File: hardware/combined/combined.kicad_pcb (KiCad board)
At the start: 2 copper layers, 62.1 x 208.5 mm, 143 parts, among them J1 USB-C 5V in, J2 Mini-DIN-8 to printer, J4 Mini-DIN-8 LocalTalk, SW1 EVQP44B3M, SW2 B3U-1000P, SW3 TS-1002-BR16026, U1 ESP32-S3-WROOM-1-N8R2, U2 SP3490EN-L, U3 SP3232EEN, U4 AP7361C-33E, U5 USBLC6-2SC6, U6 SP3485EN-L, U7 PIC12F1840-I/P, U8 SP3485EN-L, U9 74AHCT1G125SE-7

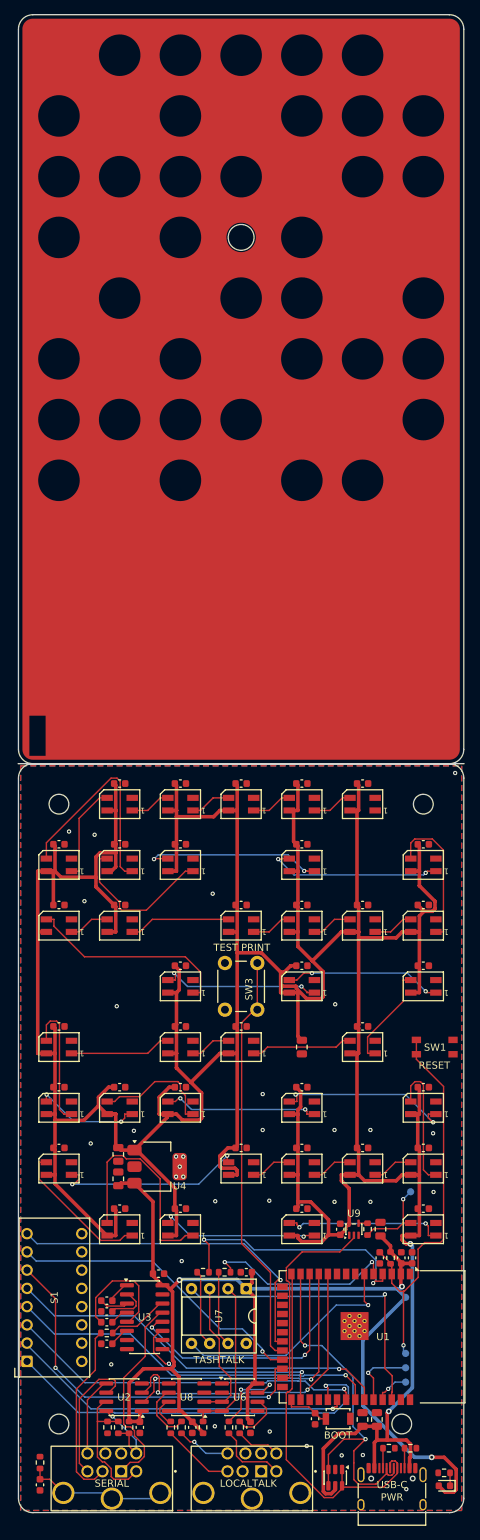
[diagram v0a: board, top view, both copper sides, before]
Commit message: Panel: test hole 3.6 -> 3.8mm for the TS-1002's 3.5+/-0.2mm shaft
Datasheet-verified: the switch is 16.0mm tall (correct for 0.5-1mm proud at
a 13.4-13.9mm lattice) but its shaft is 3.5mm — 3.6 left 0.05mm/side and a
tolerance-stack bind. Wells chose the bigger hole over a printed plunger.
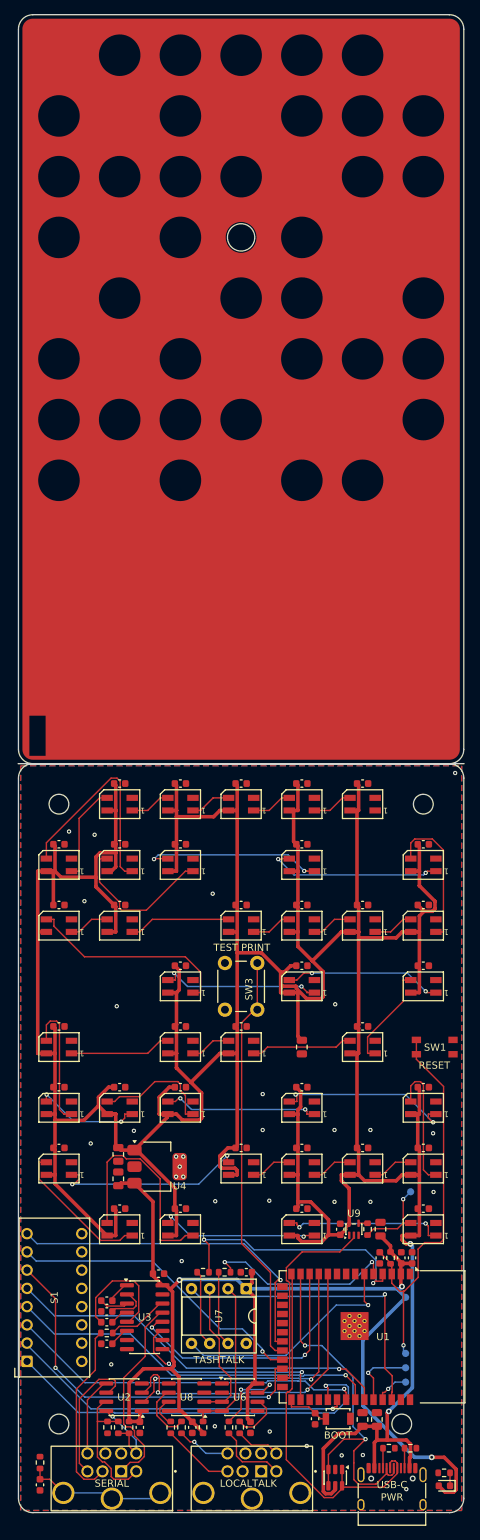
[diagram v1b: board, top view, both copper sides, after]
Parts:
- moved MT1 50.7 mm to (156.4, -38.6)
- moved MT2 50.7 mm to (105.6, -38.6)
- moved MT3 47.7 mm to (156.4, 47.7)
- moved MT4 47.7 mm to (108.6, 47.7)
- renumbered MT2 to MT1, MT1 to MT2, MT4 to MT3, MT3 to MT4

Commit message: Panel: Frame 26 test dot — squared gold tab, glyphs clear of the 3.8mm hole
Wells redrew the test dot for the bigger hole: gold teardrop (disc + rounded
SE tab), hole marker at 3.83mm, 'test' knockout letters moved onto the tab.
Generator changes to carry it: knockout ownership reach 1.45r (glyphs live
past the disc edge now), glyph subtraction by boolean (edge-crossing holes
voided the whole opening), gold copper clipped around the NPTH, gold-art
mask opening keeps mask over knockout strokes.
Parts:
- moved MT1 98.6 mm to (156.4, -38.6)
- moved MT4 98.6 mm to (108.6, 47.7)
- renumbered MT4 to MT1, MT1 to MT4

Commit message: Panel: black ring around the test hole + repositioned glyphs (Frame 26 rev 2)
Mask now stays closed inside the black marker circle (3.83mm), so the
drill's surround reads black instead of a bare-FR4 cream ring; marker
diameter rides in panel_layout.json as hole_mark_dia. Wells's updated
export pulls the glyphs 3px left so the final t clears the tab edge.
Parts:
- moved MT1 98.6 mm to (156.4, -38.6)
- moved MT3 86.3 mm to (156.4, 47.7)
- moved MT4 47.7 mm to (108.6, 47.7)
- renumbered MT4 to MT1, MT1 to MT3, MT3 to MT4

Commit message: Panel: close mask to the copper edge around the test hole — no FR4 sliver
The marker circle (3.83mm) sits inside the hole-clearance floor (copper
can't start before 4.4mm), so keeping mask closed only to the marker left
a 0.3mm bare-FR4 ring. Mask now closes to max(marker, hole+0.6): the black
ring runs from drill to gold with nothing between.
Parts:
- moved MT2 100.1 mm to (105.6, -38.6)
- moved MT3 100.1 mm to (156.4, 47.7)
- moved MT1 98.6 mm to (156.4, -38.6)
- moved MT4 98.6 mm to (108.6, 47.7)
- renumbered MT4 to MT1, MT3 to MT2, MT2 to MT3, MT1 to MT4

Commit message: Revert "Panel: close mask to the copper edge around the test hole — no FR4 sliver"
This reverts commit eb9a4d2783863aab7f219a44ac207152b572bd98.
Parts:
- moved MT2 100.1 mm to (105.6, -38.6)
- moved MT3 100.1 mm to (156.4, 47.7)
- moved MT1 98.6 mm to (156.4, -38.6)
- moved MT4 98.6 mm to (108.6, 47.7)
- renumbered MT4 to MT1, MT3 to MT2, MT2 to MT3, MT1 to MT4

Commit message: Regenerate fab outputs after the mask-edge revert
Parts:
- moved MT1 98.6 mm to (156.4, -38.6)
- moved MT4 98.6 mm to (108.6, 47.7)
- renumbered MT4 to MT1, MT1 to MT4

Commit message: Regenerate panel, combined panel and fab packages
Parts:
- moved MT2 100.1 mm to (105.6, -38.6)
- moved MT3 100.1 mm to (156.4, 47.7)
- renumbered MT3 to MT2, MT2 to MT3

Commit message: Pre-order review #2: stitch 10 stranded GND islands, H4 and VBUS via fixes, CAM-clean seam, CTS invert option
Ten top-side GND islands (SP3490, both SP3485 grounds, LED 20 onward, the WROOM's
100 nF caps, CC1's pulldown, SP3232 V+ cap and T2IN tie) had no via to the plane.
KiCad reported them as Zone<->Zone unconnected items and the 08-22 review had
classed those as benign. Twelve vias and three short bottom-side jogs (VBUS trunk
by U1, 3V3 diagonal and VBUS via at H4, DIP5 diagonal by U3) bring the GND net
to one cluster; DRC is 0 errors / 0 unconnected with schematic parity.

Also: second via on the 5 V layer crossing by U1/D10; V-CUT score line and label
moved from Edge.Cuts to User.Comments; H_TEST excluded from pos/BOM; make_fab.sh
regenerates the PCBWay package; firmware gains CONFIG_AIRWRITER_INVERT_CTS and the
serial_out CTS comment now matches the code. Report: docs/review-2026-08-25-pre-order-2.md
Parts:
- moved MT2 100.1 mm to (105.6, -38.6)
- moved MT1 98.6 mm to (156.4, -38.6)
- moved MT4 86.3 mm to (108.6, 47.7)
- moved MT3 86.3 mm to (156.4, 47.7)
- renumbered MT4 to MT1, MT3 to MT2, MT1 to MT3, MT2 to MT4
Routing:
- net /VBUS: track 600.0 -> 601.5 mm, vias 2 -> 3
- net /GND: vias 32 -> 43
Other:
- board size 62.1 x 208.5 mm -> 62 x 208.5 mm
